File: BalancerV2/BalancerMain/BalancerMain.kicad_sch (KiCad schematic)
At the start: 56 parts, among them J1 BATT 3S +/-, J2 BANNER bn/bu/wh, J3 MPU + / -, J4 GPS 3V3/GND/RX/TX, J6 ADXL357 P1, J7 ADXL357 P2, J8 DOCK pogo 5V/GND/DET, Q1 AO3400A, Q2 AO3401A, SW1 ACQUIRE, U1 FeatherS3[D], U2 TPS54202DDCR, U3 MT3608, U4 LM1815MX/NOPB

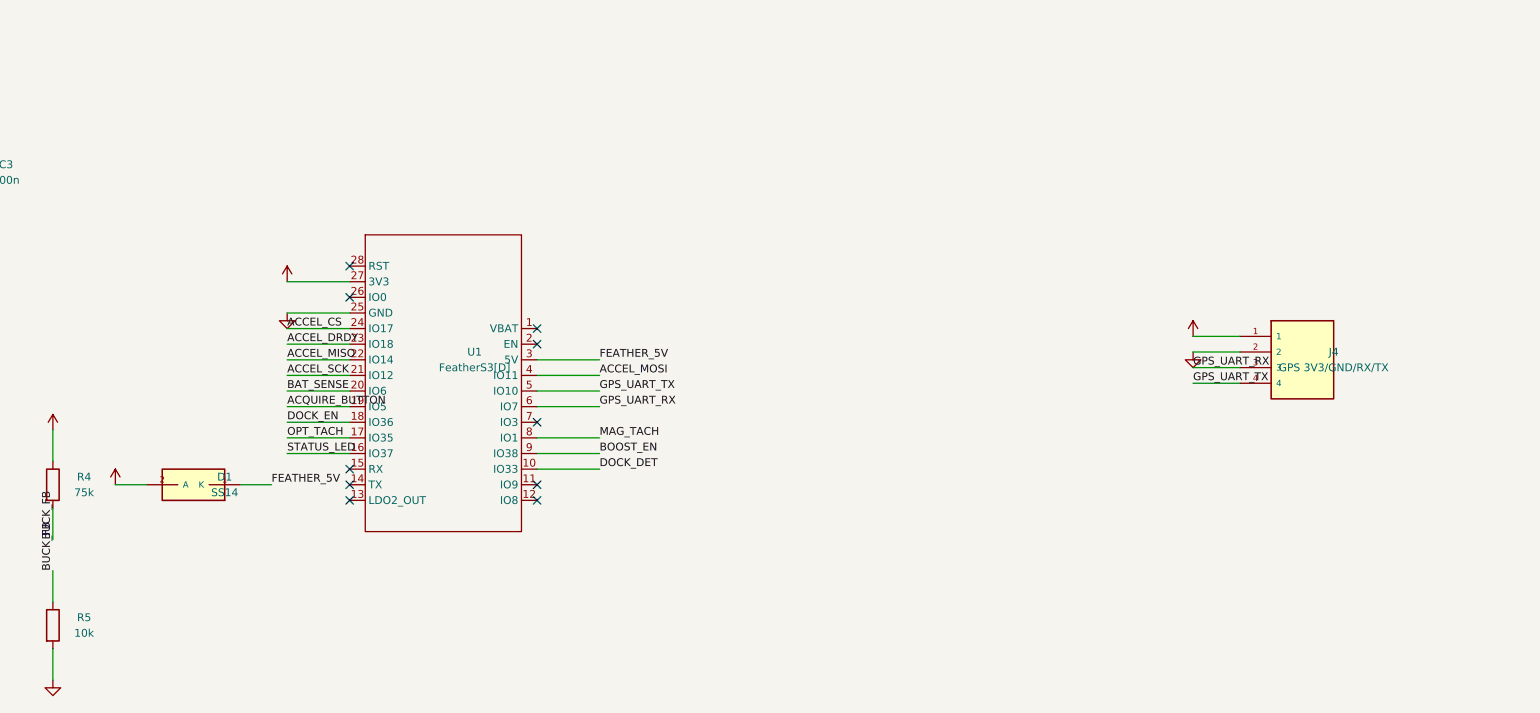
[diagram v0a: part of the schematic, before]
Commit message: v2 main unit: OMGS3 module on pads replaces the FeatherS3
Official Unexpected Maker symbol and footprint copied under
BalancerMain/vendor with their CERN OHL license. New GPIO map, PROG
header for USB D+/D-, IO0 and RESET, 5 V OR-ing diode removed. Board
regenerated with the module's antenna end at the board edge and the
LED moved off it. Pin map and design notes updated.

Co-Authored-By: Claude Fable 5.1 <noreply@anthropic.com>
Claude-Session: https://claude.ai/code/session_01XT5akMmBgbqYX83ryU4fFA
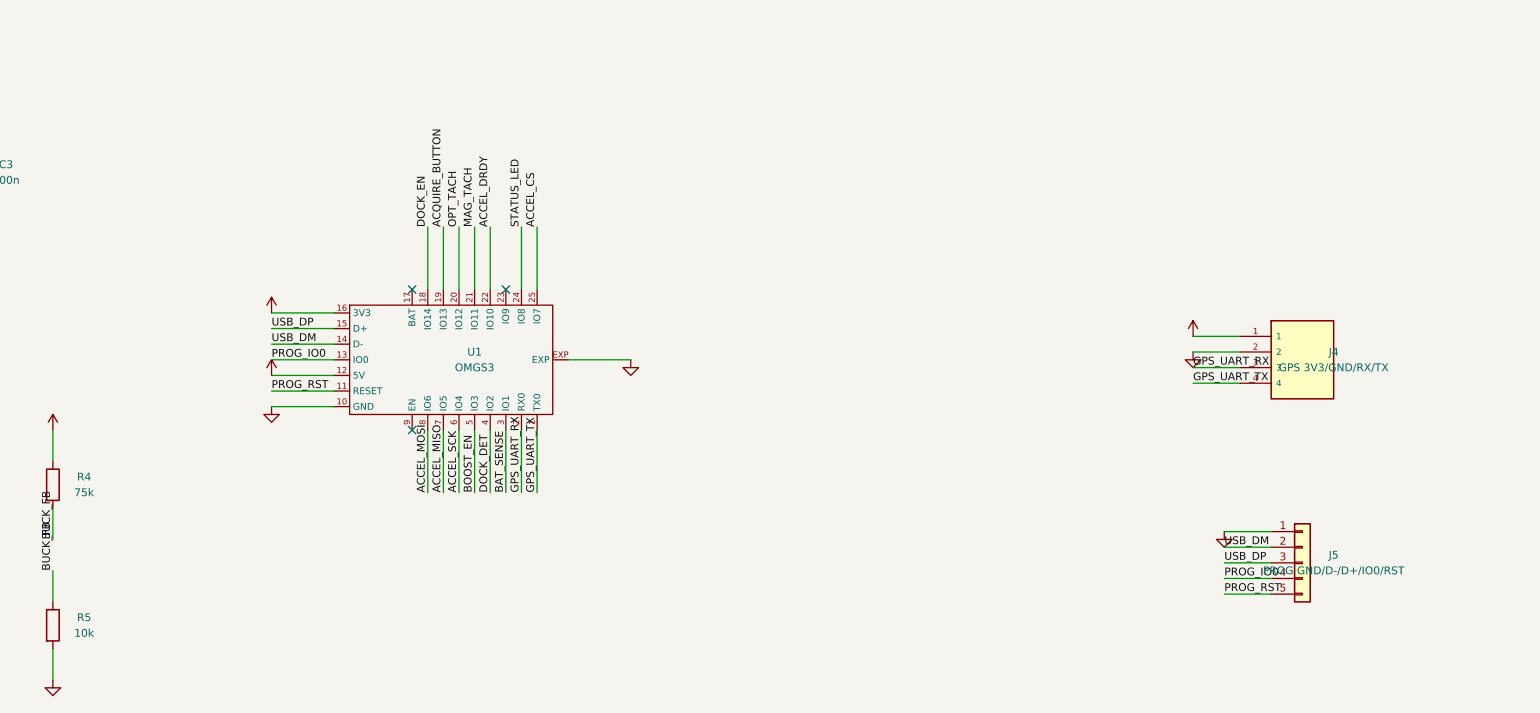
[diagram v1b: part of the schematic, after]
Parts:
- removed D1: SS14, Diode_SMD:D_SMA, symbol BalancerMain:D_Schottky
- removed U1: FeatherS3[D], BalancerMain:FeatherS3, symbol BalancerMain:FeatherS3
- added J5: PROG GND/D-/D+/IO0/RST, Connector_PinHeader_2.54mm:PinHeader_1x05_P2.54mm_Vertical, symbol Connector_Generic:Conn_01x05
- added U1: OMGS3, BalancerMain:OMGS3, symbol BalancerMain:OMGS3
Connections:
- net +3V3: now also U1.16 (3V3)
- net +5V: now also U1.12 (5V)
- net ACCEL_CS: now also U1.25 (IO7)
- net ACCEL_DRDY: now also U1.22 (IO10)
- net ACCEL_MISO: now also U1.7 (IO5)
- net ACCEL_MOSI: now also U1.8 (IO6)
- net ACCEL_SCK: now also U1.6 (IO4)
- net ACQUIRE_BUTTON: now also U1.19 (IO13)
- net BAT_SENSE: now also U1.3 (IO1)
- net BOOST_EN: now also U1.5 (IO3)
- net DOCK_DET: now also U1.4 (IO2)
- net DOCK_EN: now also U1.18 (IO14)
- net GND: now also J5.1 (Pin_1), U1.10 (GND), U1.EXP
- net GPS_UART_RX: now also U1.2 (RX0)
- net GPS_UART_TX: now also U1.1 (TX0)
- net MAG_TACH: now also U1.21 (IO11)
- net OPT_TACH: now also U1.20 (IO12)
- net STATUS_LED: now also U1.24 (IO8)
- new net PROG_IO0: J5.4 (Pin_4), U1.13 (IO0)
- new net PROG_RST: J5.5 (Pin_5), U1.11 (RESET)
- new net USB_DM: J5.2 (Pin_2), U1.14 (D-)
- new net USB_DP: J5.3 (Pin_3), U1.15 (D+)
- no-connect marks 21 -> 14

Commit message: v2 main unit: 1S LiPo on the OMGS3 charger, USB-C, 12 V boost only for the Banner
Removes the 3S input, buck, battery divider and dock switch. Adds JST-PH
cell connector, USB-C 16P (Unexpected Maker's footprint and wiring from
their OMGS3 carrier), CC resistors, VBUS Schottky, 1x03 IO0/RST header.
Board is 70 x 64 mm with 41 footprints; netlist check passes (33 nets).

Co-Authored-By: Claude Fable 5.1 <noreply@anthropic.com>
Claude-Session: https://claude.ai/code/session_01XT5akMmBgbqYX83ryU4fFA
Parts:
- removed C3, C4: 100n, Capacitor_SMD:C_1206_3216Metric, symbol Device:C
- removed C5, C6: 10u 25V, Capacitor_SMD:C_1206_3216Metric, symbol Device:C
- removed D3: SS14, Diode_SMD:D_SMA, symbol BalancerMain:D_Schottky
- removed F1: 2A polyfuse 1812, Fuse:Fuse_1812_4532Metric, symbol BalancerMain:Polyfuse
- removed J1: BATT 3S +/-, BalancerMain:SolderWire_1x02, symbol Connector_Generic:Conn_01x02
- removed J5: PROG GND/D-/D+/IO0/RST, Connector_PinHeader_2.54mm:PinHeader_1x05_P2.54mm_Vertical, symbol Connector_Generic:Conn_01x05
- removed J8: DOCK pogo 5V/GND/DET, BalancerMain:Pogo_1x03, symbol BalancerMain:Conn_01x03
- removed L1: 10uH 3A, BalancerMain:L_Radial_D9_P5, symbol Device:L
- removed Q1: AO3400A, Package_TO_SOT_SMD:SOT-23, symbol Transistor_FET:AO3400A
- removed Q2: AO3401A, Package_TO_SOT_SMD:SOT-23, symbol Transistor_FET:AO3401A
- removed R16: 1k, Resistor_SMD:R_1206_3216Metric, symbol Device:R
- removed R17, R3: 100k, Resistor_SMD:R_1206_3216Metric, symbol Device:R
- removed R18, R5: 10k, Resistor_SMD:R_1206_3216Metric, symbol Device:R
- removed R4: 75k, Resistor_SMD:R_1206_3216Metric, symbol Device:R
- removed U2: TPS54202DDCR, Package_TO_SOT_SMD:SOT-23-6, symbol BalancerMain:TPS54202DDCR
- added D1: SS14, Diode_SMD:D_SMA, symbol BalancerMain:D_Schottky
- added J1: LIPO 1S JST-PH, BalancerMain:JST_PH_1x02_Vertical, symbol BalancerMain:JST_PH_1x02
- added J5: PROG GND/IO0/RST, Connector_PinHeader_2.54mm:PinHeader_1x03_P2.54mm_Vertical, symbol BalancerMain:Conn_01x03
- added J9: USB-C 16P, BalancerMain:USB_C_16P, symbol BalancerMain:USB_C_16P
- R1: value 100k -> 5.1k
- R2: value 10k -> 5.1k
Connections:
- net GND: now also R1.2, J1.2, J5.1, J9.GND, J9.GND2 (GND), J9.SHLD (SHIELD)
- net PROG_IO0: now also J5.2
- net PROG_RST: now also J5.3
- net USB_DM: now also J9.A7 (D-), J9.B7 (D-)
- net USB_DP: now also J9.A6 (D+), J9.B6 (D+)
- net VBAT: now also U1.17 (BAT), J1.1; no longer C2.1, R1.1
- net +5V renamed MOD_5V
- net MOD_5V: now also C2.1, D1.1 (K)
- removed net BAT_SENSE: R1.2, R2.1, U1.3 (IO1)
- net DOCK_DET: no longer names the net of U1.4 (IO2)
- net DOCK_EN: no longer names the net of U1.18 (IO14)
- new net USB_CC1: J9.A5 (CC1), R1.1
- new net USB_CC2: J9.B5 (CC2), R2.1
- new net VBUS: D1.2 (A), J9.VBUS1 (VBUS), J9.VBUS2 (VBUS)
- no-connect marks 14 -> 16

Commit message: v2 main unit: status LED moved from IO8 to IO14, fuel-gauge I2C left free
Co-Authored-By: Claude Fable 5.1 <noreply@anthropic.com>
Claude-Session: https://claude.ai/code/session_01XT5akMmBgbqYX83ryU4fFA
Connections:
- net STATUS_LED: now also U1.18 (IO14); no longer U1.24 (IO8)
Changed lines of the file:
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@@
+	(wire
+		(pts
+			(xy 251.46 90.17)
+			(xy 251.46 80.01)
+		)
+		(stroke
+			(width 0)
+			(type default)
+		)
+	)
 	(wire
 		(pts
@@
 	(wire
 		(pts
-			(xy 266.7 90.17)
-			(xy 266.7 80.01)
-		)
-		(stroke
-			(width 0)
-			(type default)
-		)
-	)
-	(wire
-		(pts
 			(xy 269.24 90.17)
 			(xy 269.24 80.01)
@@
 	)
 	(no_connect
-		(at 251.46 90.17)
-	)
-	(no_connect
 		(at 264.16 90.17)
+	)
+	(no_connect
+		(at 266.7 90.17)
 	)
 	(no_connect
@@
 		)
 	)
+	(label "STATUS_LED"
+		(at 251.46 80.01 90)
+		(effects
+			(font
+				(size 1.27 1.27)
+			)
+			(justify left bottom)
+		)
+	)
 	(label "ACQUIRE_BUTTON"
 		(at 254.0 80.01 90)
@@
 		(effects
 			(font
-				(size 1.27 1.27)
-			)
-			(justify left bottom)
-		)
-	)
-	(label "STATUS_LED"
-		(at 266.7 80.01 90)
-		(effects
-			(font

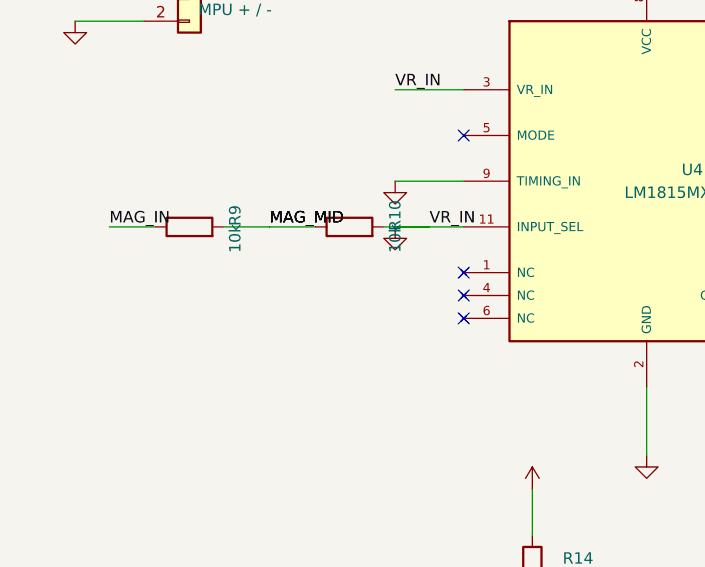
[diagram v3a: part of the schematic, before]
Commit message: v2 main unit: fix ERC errors (R10 stub overlapping LM1815 ground, VBUS pin types, rail symbol lib names); netlist check now flags overlapping wires and stacked labels
Co-Authored-By: Claude Fable 5.1 <noreply@anthropic.com>
Claude-Session: https://claude.ai/code/session_01XT5akMmBgbqYX83ryU4fFA
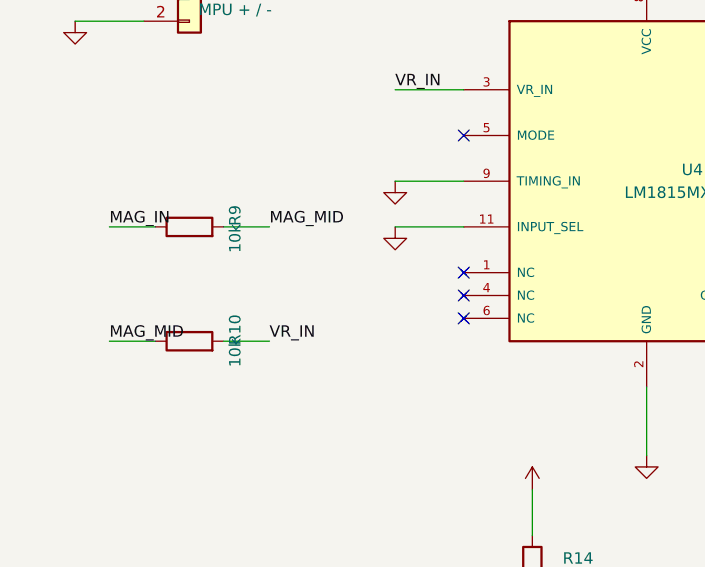
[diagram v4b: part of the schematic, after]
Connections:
- net GND: no longer R10.2, U4.3 (VR_IN)
- new net VR_IN: R10.2, U4.3 (VR_IN)
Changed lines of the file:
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@@
 	(wire
 		(pts
-			(xy 39.37 271.78)
-			(xy 34.29 271.78)
+			(xy 21.59 284.48)
+			(xy 16.51 284.48)
 		)
 		(stroke
@@
 	(wire
 		(pts
-			(xy 46.99 271.78)
-			(xy 52.07 271.78)
+			(xy 29.21 284.48)
+			(xy 34.29 284.48)
 		)
 		(stroke
@@
 	)
 	(label "MAG_MID"
-		(at 34.29 271.78 180)
+		(at 16.51 284.48 180)
 		(effects
 			(font
@@
 	)
 	(label "VR_IN"
-		(at 52.07 271.78 0)
+		(at 34.29 284.48 0)
 		(effects
 			(font
@@
 	)
 	(symbol
-		(lib_id "power:VBAT")
+		(lib_id "BalancerMain:VBAT")
 		(at 248.92 80.01 0)
 		(unit 1)
@@
 	)
 	(symbol
-		(lib_id "power:VBAT")
+		(lib_id "BalancerMain:VBAT")
 		(at 7.62 48.26 0)
 		(unit 1)
@@
 	)
 	(symbol
-		(lib_id "power:VBAT")
+		(lib_id "BalancerMain:VBAT")
 		(at 50.8 45.72 0)
 		(unit 1)
@@
 	)
 	(symbol
-		(lib_id "power:VBAT")
+		(lib_id "BalancerMain:VBAT")
 		(at 71.12 52.07 0)
 		(unit 1)
@@
 	)
 	(symbol
-		(lib_id "power:VBUS")
+		(lib_id "BalancerMain:VBUS")
 		(at 104.14 111.76 0)
 		(unit 1)
@@
 	)
 	(symbol
-		(lib_id "power:VBUS")
+		(lib_id "BalancerMain:VBUS")
 		(at 104.14 114.3 0)
 		(unit 1)
@@
 	)
 	(symbol
-		(lib_id "power:VBUS")
+		(lib_id "BalancerMain:VBUS")
 		(at 157.48 109.22 0)
 		(unit 1)
@@
 	)
 	(symbol
-		(lib_id "power:VBUS")
+		(lib_id "BalancerMain:VBUS")
 		(at 177.8 99.06 0)
 		(unit 1)
@@
 	)
 	(symbol
-		(lib_id "power:VBAT")
+		(lib_id "BalancerMain:VBAT")
 		(at 53.34 182.88 0)
 		(unit 1)
@@
 	)
 	(symbol
-		(lib_id "power:VBAT")
+		(lib_id "BalancerMain:VBAT")
 		(at 107.95 177.8 0)
 		(unit 1)
@@
 	)
 	(symbol
-		(lib_id "power:+12V")
+		(lib_id "BalancerMain:+12V")
 		(at 154.94 177.8 0)
 		(unit 1)
@@
 	)
 	(symbol
-		(lib_id "power:+12V")
+		(lib_id "BalancerMain:+12V")
 		(at 157.48 191.77 0)
 		(unit 1)
@@
 	)
 	(symbol
-		(lib_id "power:+12V")
+		(lib_id "BalancerMain:+12V")
 		(at 177.8 179.07 0)
 		(unit 1)
@@
 	)
 	(symbol
-		(lib_id "power:+12V")
+		(lib_id "BalancerMain:+12V")
 		(at 157.48 177.8 0)
 		(unit 1)
@@
 	(symbol
 		(lib_id "Device:R")
-		(at 43.18 271.78 90)
+		(at 25.4 284.48 90)
 		(unit 1)
 		(exclude_from_sim no)
@@
 		(dnp no)
 		(property "Reference" "R10"
-			(at 48.26 270.51 0)
+			(at 30.479999999999997 283.21000000000004 0)
 			(effects
 				(font
@@
 		)
 		(property "Value" "10k"
-			(at 48.26 273.04999999999995 0)
+			(at 30.479999999999997 285.75 0)
 			(effects
 				(font
@@
 		)
 		(property "Footprint" "Resistor_SMD:R_1206_3216Metric"
-			(at 43.18 271.78 0)
+			(at 25.4 284.48 0)
 			(effects
 				(font
@@
 		)
 		(property "Datasheet" ""
-			(at 43.18 271.78 0)
+			(at 25.4 284.48 0)
 			(effects
 				(font
@@
 	)
 	(symbol
-		(lib_id "power:+12V")
+		(lib_id "BalancerMain:+12V")
 		(at 7.62 320.04 0)
 		(unit 1)
